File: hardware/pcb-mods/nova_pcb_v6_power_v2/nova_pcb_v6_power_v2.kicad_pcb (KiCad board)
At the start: 4 copper layers, 112 x 90 mm, 61 parts, among them J1 XT60_4S_IN, J12 XT30_JET_12V, J13 XT30_L2_12V, J14 XT30_Arm7V5, J2 UBEC_5V_AUX, J20 IB_2x06, J3 XT30_Inj, J4 XT30_Inj, J5 XT30_Inj, J6 XT30_Inj, J7 XT30_Inj, J8 ServoBus_TTL, M1 Voltmeter_DC, Q1 IRLB3034PBF, Q2 BSS138_cutoff, Q3 BSS138_estop, Q4 BSS138_jetcut, SW1 Rocker_30A, SW2 Estop_NC_latching, U1 Pololu_D42V110F7_LEG_7V5, U10 INA226, U11 INA226, U12 INA226, U2 Pololu_D42V110F12_HIP_12V, U3 Pololu_D24V22F12_L2_12V, U4 Pololu_D42V55F12_JET_12V, U5 Pololu_D42V55F7_ARM_7V5, U8 LM393, U9 INA226

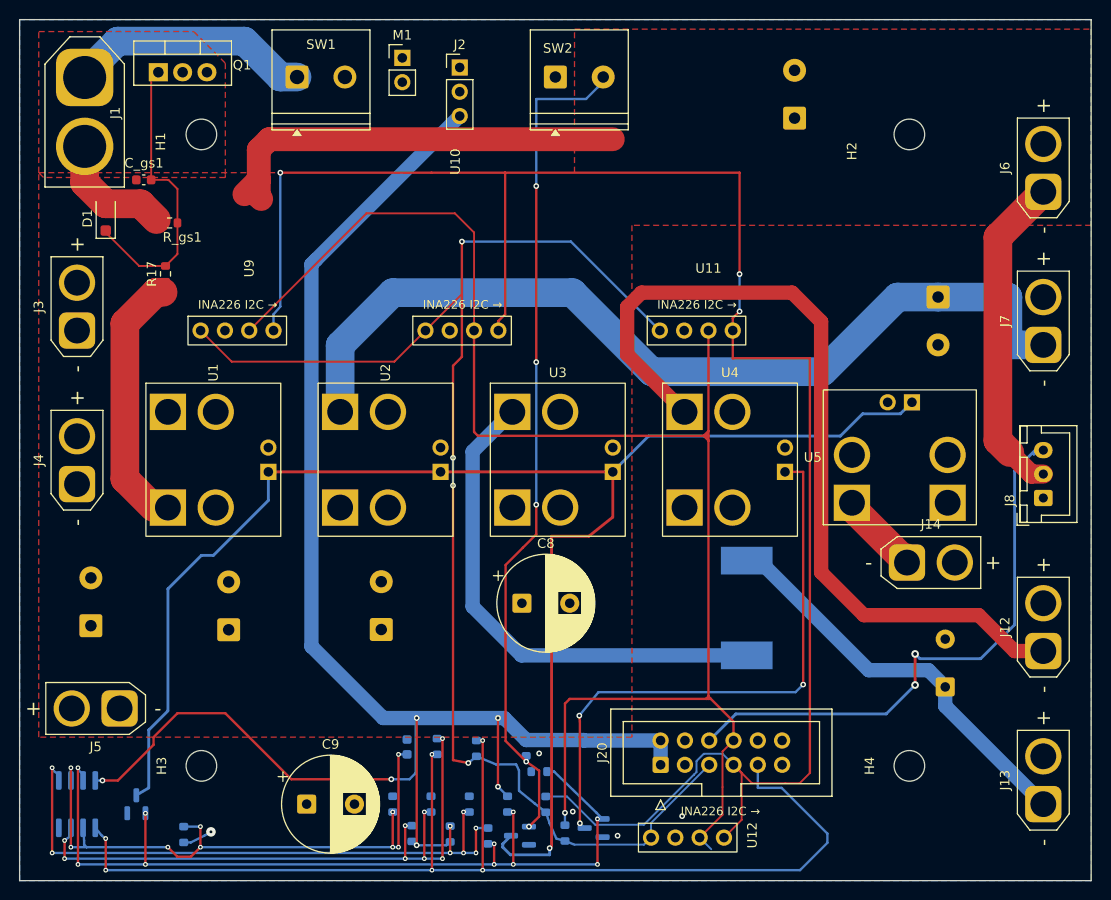
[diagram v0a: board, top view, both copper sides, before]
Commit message: power board: pour VBAT + V12_HIP on B.Cu (high-current heat-spread)
Added B.Cu copper pours on the two non-plane-backed high-current rails flagged
in pre-fab review: VBAT (raw battery feed ~14A/30A peak) and V12_HIP (hip rail
~8-9A, ~20A stall) — previously 3mm trace only. Thermal-relief connection
(1.0mm spokes / 0.3mm gap) keeps the THT pads hand-solderable (Pinecil); the
3mm traces stay in parallel. Priority 10 claims only GND-background bottom
copper (GND return carried by the GND.Cu inner plane, so no starvation).
B.Cu copper +9%. DRC 0 hard / 0 unconnected, fab_gate GO. SW1 1.5mm preserved.

Co-Authored-By: Claude Opus 4.8 <noreply@anthropic.com>
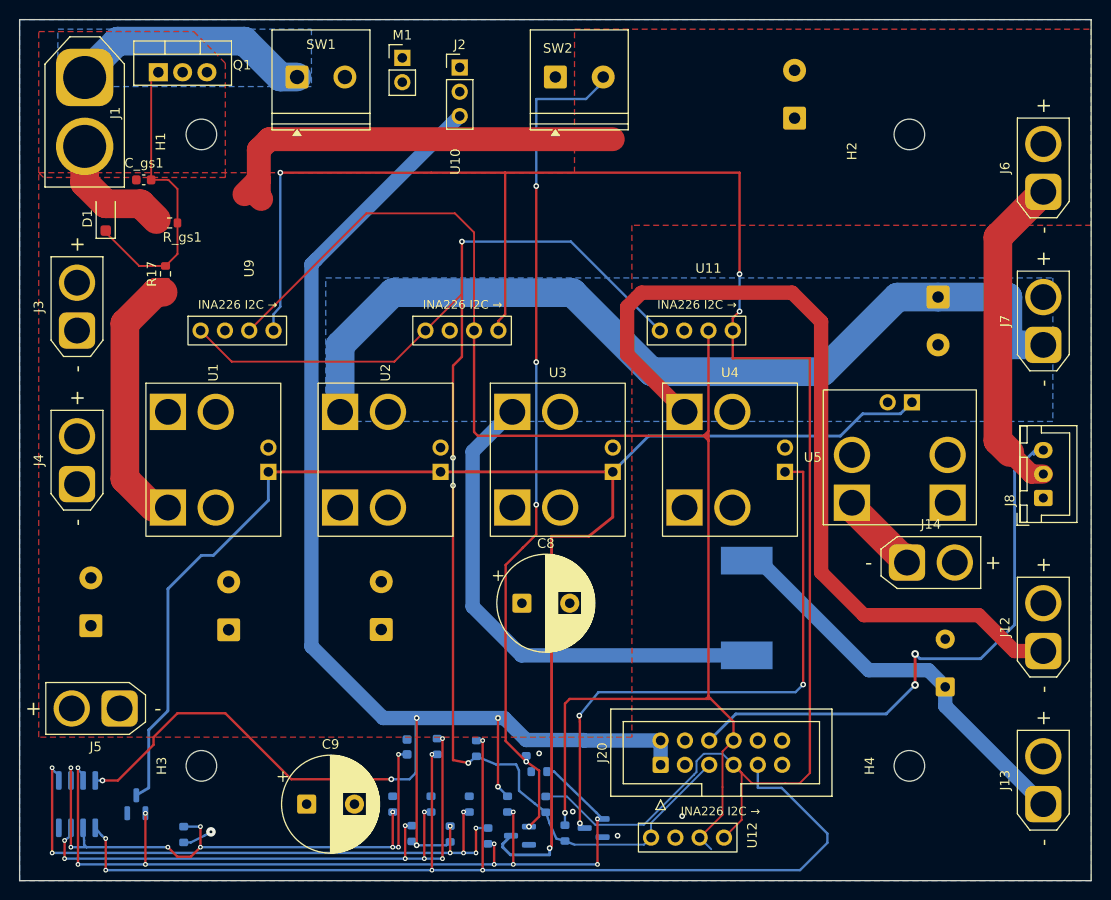
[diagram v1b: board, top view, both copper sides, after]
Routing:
- added copper zone on B.Cu, net /01 Battery Input + Reverse Protection/VBAT
- added copper zone on B.Cu, net V12_HIP
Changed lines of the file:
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@@
+	)
+	(zone
+		(net 5)
+		(net_name "/01 Battery Input + Reverse Protection/VBAT")
+		(layer "B.Cu")
+		(name "VBAT_pour")
+		(hatch edge 0.5)
+		(priority 10)
+		(connect_pads
+			(clearance 0.5)
+		)
+		(min_thickness 0.25)
+		(filled_areas_thickness no)
+		(fill yes
+			(thermal_gap 0.3)
+			(thermal_bridge_width 1)
+		)
+		(polygon
+			(pts
+				(xy 88 52) (xy 114.5 52) (xy 114.5 58) (xy 88 58)
+			)
+		)
 	)
 	(zone
@@
 			)
 		)
+	)
+	(zone
+		(net 3)
+		(net_name "V12_HIP")
+		(layer "B.Cu")
+		(name "V12_HIP_pour")
+		(hatch edge 0.5)
+		(priority 10)
+		(connect_pads
+			(clearance 0.5)
+		)
+		(min_thickness 0.25)
+		(filled_areas_thickness no)
+		(fill yes
+			(thermal_gap 0.3)
+			(thermal_bridge_width 1)
+		)
+		(polygon
+			(pts
+				(xy 116 78) (xy 192 78) (xy 192 93) (xy 116 93)
+			)
+		)

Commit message: power board: bump via annular for PCBWay 2oz margin (0.5→0.55mm pads)
Pre-fab review flagged 41 vias at 0.125mm annular (0.25/0.5mm) — ~5µm under
PCBWay's 0.13mm nominal. Bumped pads 0.5→0.55mm (annular 0.15mm, clears spec).
2 vias in the dense safety-chain cluster (VSENSE/HARDCUT, 0.74mm apart) kept at
0.5mm where 0.55 broke the 0.2mm clearance — acceptable, within PCBWay absolute
capability. Drills unchanged (0.25mm). Refilled, regen gerbers. DRC 0 errors /
0 unconnected, fab_gate GO. SW1 1.5mm preserved.

Co-Authored-By: Claude Opus 4.8 <noreply@anthropic.com>
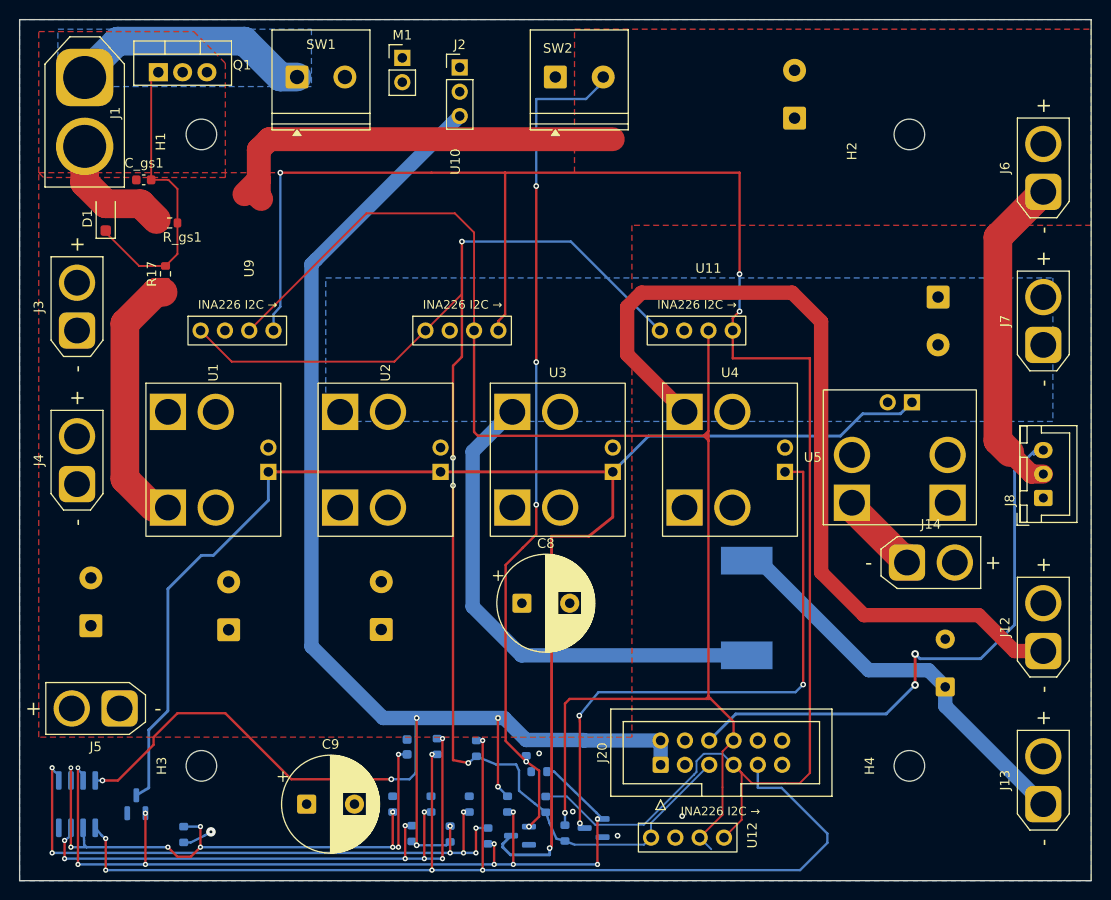
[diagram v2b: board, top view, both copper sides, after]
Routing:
- net V12_HIP: track 94.4 -> 0.00 mm

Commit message: power board: SW1 value Rocker_30A → Contura_SPST_18A (real part)
Footprint value was a misleading "Rocker_30A"; actual switch is the Blue Sea
Contura SPST (~18A @ 16.8V). Cosmetic F.Fab label only (not in gerber layers);
regen for fab_gate freshness. SW1 drill 1.5mm preserved, fab_gate GO.

Co-Authored-By: Claude Opus 4.8 <noreply@anthropic.com>
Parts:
- SW1: value Rocker_30A -> Contura_SPST_18A
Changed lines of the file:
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@@
 			)
 		)
-		(property "Value" "Rocker_30A"
+		(property "Value" "Contura_SPST_18A"
 			(at 2.5 6.52 90)
 			(layer "F.Fab")
